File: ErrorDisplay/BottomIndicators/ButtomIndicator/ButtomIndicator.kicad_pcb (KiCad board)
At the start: 2 copper layers, 163.3 x 15 mm, 0 parts

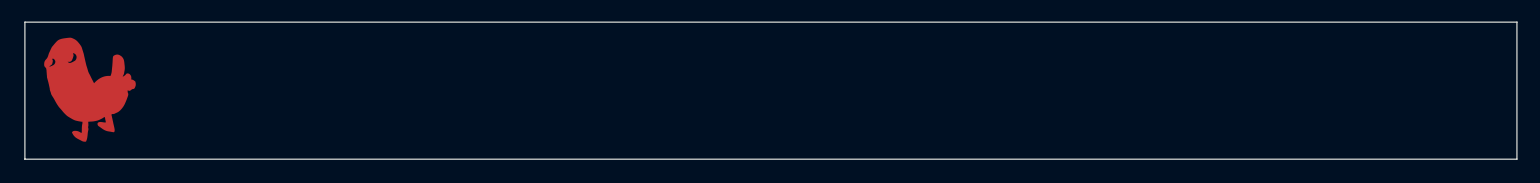
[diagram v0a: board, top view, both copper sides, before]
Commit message: Some placements, adding plastic inserts.
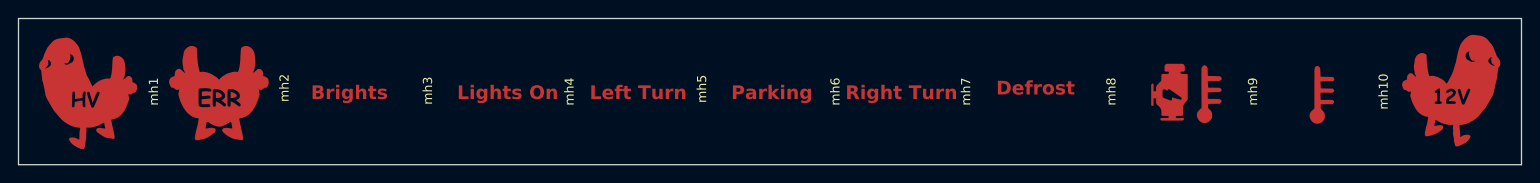
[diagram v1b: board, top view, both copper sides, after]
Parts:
- added mh1: MountingHole, Library:PlasticInsert, F.Cu at (81.3, 108.5)
- added mh10: MountingHole, Library:PlasticInsert, F.Cu at (215.9, 108.5)
- added mh2: MountingHole, Library:PlasticInsert, F.Cu at (95.6, 108.5)
- added mh3: MountingHole, Library:PlasticInsert, F.Cu at (111.2, 108.5)
- added mh4: MountingHole, Library:PlasticInsert, F.Cu at (126.9, 108.5)
- added mh5: MountingHole, Library:PlasticInsert, F.Cu at (141.4, 108.5)
- added mh6: MountingHole, Library:PlasticInsert, F.Cu at (155.9, 108.5)
- added mh7: MountingHole, Library:PlasticInsert, F.Cu at (170.4, 108.5)
- added mh8: MountingHole, Library:PlasticInsert, F.Cu at (186.1, 108.5)
- added mh9: MountingHole, Library:PlasticInsert, F.Cu at (201.6, 108.5)
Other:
- board size 163.3 x 15 mm -> 164.5 x 16 mm
- board text added: "Brights"
- board text added: "Defrost"
- board text added: "Left Turn"
- board text added: "Lights On"
- board text added: "Parking"
- board text added: "Right Turn"

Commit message: Added all SVGs imported. Need to invert all.
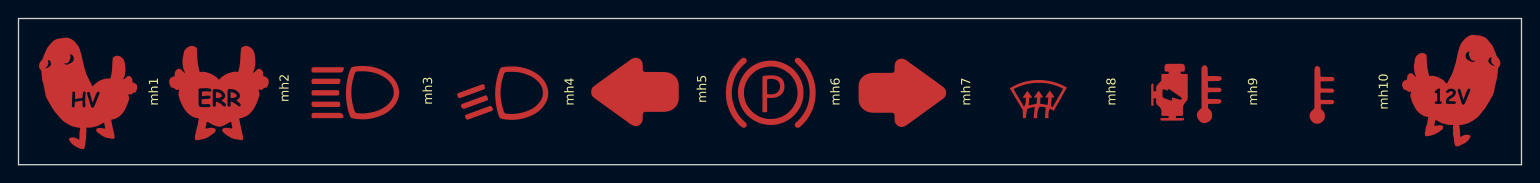
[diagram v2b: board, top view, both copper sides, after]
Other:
- board text removed: "Brights"
- board text removed: "Defrost"
- board text removed: "Left Turn"
- board text removed: "Lights On"
- board text removed: "Parking"
- board text removed: "Right Turn"

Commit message: Placement and positioning of icons
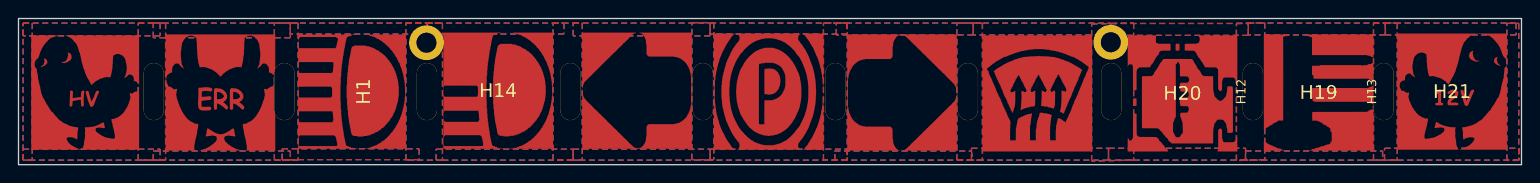
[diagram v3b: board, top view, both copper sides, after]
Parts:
- removed mh1, mh10, mh2, mh3, mh4, mh5, mh6, mh7, mh8, mh9: MountingHole, Library:PlasticInsert
- added H1: MountingHole_Pad, Library:brights, F.Cu at (103.0, 108.5)
- added H10: MountingHole_Pad, Library:PlasticInsert, F.Cu at (170.4, 108.5)
- added H11: MountingHole_Pad, Library:PlasticInsert, F.Cu at (186.1, 108.5)
- added H12: MountingHole_Pad, Library:PlasticInsert, F.Cu at (201.6, 108.5)
- added H13: MountingHole_Pad, Library:PlasticInsert, F.Cu at (215.9, 108.5)
- added H14: MountingHole_Pad, Library:lights, F.Cu at (119.0, 108.4)
- added H15: MountingHole_Pad, Library:turn, F.Cu at (134.2, 108.4)
- added H16: MountingHole_Pad, Library:parking, F.Cu at (148.6, 108.5)
- added H17: MountingHole_Pad, Library:turn, F.Cu at (163.2, 108.6)
- added H18: MountingHole_Pad, Library:defrost, F.Cu at (178.0, 108.7)
- added H19: MountingHole_Pad, Library:thermals, F.Cu at (208.8, 108.6)
- added H2: MountingHole_Pad, Library:PlasticInsert, F.Cu at (81.3, 108.5)
- added H20: MountingHole_Pad, Library:motorthermal, F.Cu at (193.9, 108.7)
- added H21: MountingHole_Pad, Library:dickbutt_12, F.Cu at (223.4, 108.5)
- added H3: MountingHole_Pad, Library:PlasticInsert, F.Cu at (95.6, 108.5)
- added H4: MountingHole_Pad, Library:PlasticInsert, F.Cu at (111.2, 108.5)
- added H5: MountingHole_Pad, Library:buttbutt, F.Cu at (88.6, 108.6)
- added H6: MountingHole_Pad, Library:dickbutt_hv, F.Cu at (73.8, 108.6)
- added H7: MountingHole_Pad, Library:PlasticInsert, F.Cu at (126.9, 108.5)
- added H8: MountingHole_Pad, Library:PlasticInsert, F.Cu at (141.4, 108.5)
- added H9: MountingHole_Pad, Library:PlasticInsert, F.Cu at (155.9, 108.5)
- added J1: Conn_01x01_Pin, MountingHole:MountingHole_2.2mm_M2_DIN965_Pad, F.Cu at (111.2, 103.2)
- added J2: Conn_01x01_Pin, MountingHole:MountingHole_2.2mm_M2_DIN965_Pad, F.Cu at (186.1, 103.1)
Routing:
- added copper zone on B.Cu, net GND
- added copper zone on F.Cu, net GND

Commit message: Proper Layout
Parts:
- moved H20 0.22 mm to (194.1, 108.6)
- moved H19 0.14 mm to (208.7, 108.7)
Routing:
- net (no net): track 0.00 -> 15.1 mm
